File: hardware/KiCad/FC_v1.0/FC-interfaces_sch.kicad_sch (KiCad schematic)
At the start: 39 parts, among them J10 PAD_OUT, J11 PAD_OUT, J12 PAD_OUT_Mini, J13 PAD_OUT_Mini, J2 MEM2061-01-188-00-A, J3 USB4105-GF-A, J4 Conn_ARM_SWD_TagConnect_TC203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, J5 SM06B-GHS-TB, J6 SM04B-GHS-TB, J7 SM06B-GHS-TB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

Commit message: Top/Bot pours
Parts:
- removed J12, J13: PAD_OUT_Mini, FC-FootprintLib:Mini_Pad_out_1x6, symbol Connector:Conn_01x06_Socket
- added J12, J13: PAD_OUT_Mini, FC-FootprintLib:Pad_out_mini_1x4, symbol Connector:Conn_01x04_Socket
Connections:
- net ADC_IN1: now also J13.4 (Pin_4)
- net ADC_IN2: now also J13.2 (Pin_2)
- net ADC_IN3: now also J13.3 (Pin_3)
- net UART5_RX: now also J12.1 (Pin_1)
- net UART5_TX: now also J12.2 (Pin_2)
- new net GPIO_68: J12.3 (Pin_3)
- new net GPIO_69: J12.4 (Pin_4)
- new net GPIO_70: J13.1 (Pin_1)

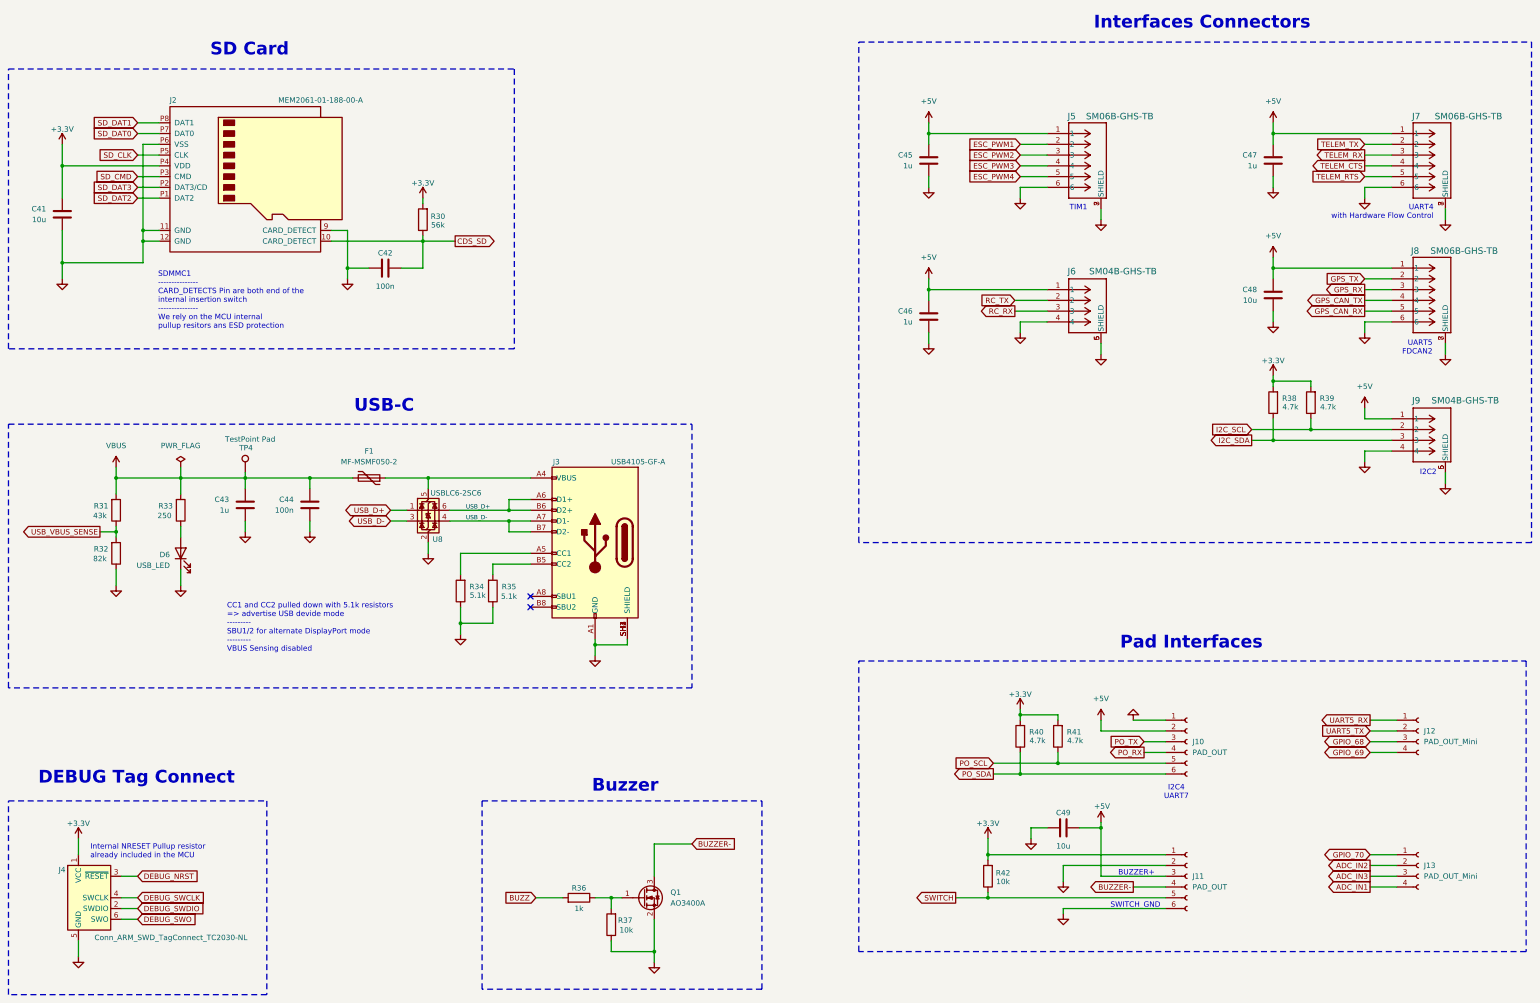
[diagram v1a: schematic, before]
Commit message: Pinout / DRC check
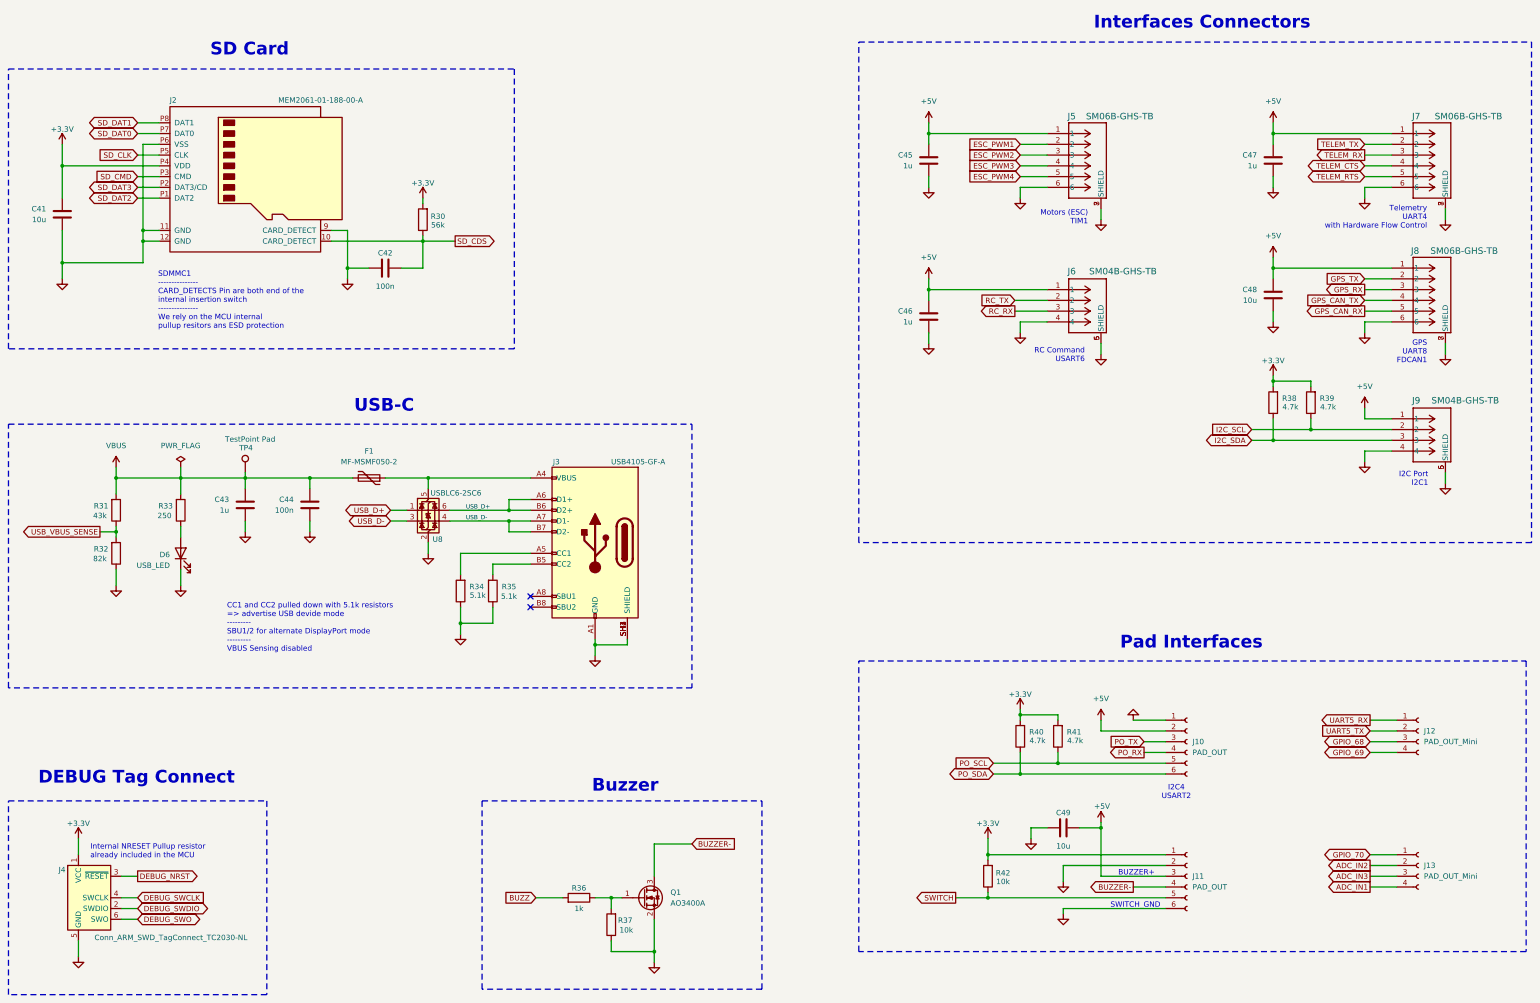
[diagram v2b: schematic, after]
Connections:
- net CDS_SD renamed SD_CDS
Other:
- note added: "GPS UART8 FDCAN1"
- note added: "I2C Port I2C1"
- note added: "I2C4 USART2"
- note added: "Motors (ESC) TIM1"
- note added: "RC Command USART6"
- note added: "Telemetry UART4 with Hardware Flow Control"
- note removed: "I2C2"
- note removed: "I2C4 UART7"
- note removed: "TIM1"
- note removed: "UART4 with Hardware Flow Control"
- note removed: "UART5 FDCAN2"
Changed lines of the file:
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@@
 	(title_block
 		(title "FC Interface Section")
-		(date "2025-12-01")
-		(rev "v0.5")
+		(date "2026-01-03")
+		(rev "v0.7")
 		(company "Guilhem Andrieu")
 	)
@@
 		)
 	)
-	(text "I2C2"
+	(text "I2C Port\nI2C1"
 		(exclude_from_sim no)
-		(at 373.126 133.35 0)
-		(effects
-			(font
-				(size 1.27 1.27)
-			)
+		(at 373.126 134.874 0)
+		(effects
+			(font
+				(size 1.27 1.27)
+			)
+			(justify right)
+		)
+	)
+	(text "RC Command\nUSART6"
+		(exclude_from_sim no)
+		(at 292.1 105.664 0)
+		(effects
+			(font
+				(size 1.27 1.27)
+			)
+			(justify right)
 		)
 	)
@@
 		)
 	)
-	(text "TIM1"
+	(text "Motors (ESC)\nTIM1"
 		(exclude_from_sim no)
-		(at 290.576 70.866 0)
-		(effects
-			(font
-				(size 1.27 1.27)
-			)
+		(at 292.862 73.152 0)
+		(effects
+			(font
+				(size 1.27 1.27)
+			)
+			(justify right)
 		)
 	)
@@
 		)
 	)
-	(text "I2C4\nUART7\n\n"
+	(text "I2C4\nUSART2\n\n"
 		(exclude_from_sim no)
 		(at 313.69 209.804 0)
@@
 		)
 	)
-	(text "UART4\nwith Hardware Flow Control"
+	(text "Telemetry\nUART4\nwith Hardware Flow Control"
 		(exclude_from_sim no)
-		(at 374.396 71.882 0)
-		(effects
-			(font
-				(size 1.27 1.27)
-			)
-			(justify right)
-		)
-	)
-	(text "UART5\nFDCAN2"
+		(at 372.872 73.152 0)
+		(effects
+			(font
+				(size 1.27 1.27)
+			)
+			(justify right)
+		)
+	)
+	(text "GPS\nUART8\nFDCAN1"
 		(exclude_from_sim no)
-		(at 374.142 103.886 0)
+		(at 372.872 104.902 0)
 		(effects
 			(font
@@
 	)
 	(global_label "SD_DAT1"
-		(shape input)
+		(shape bidirectional)
 		(at 68.58 50.8 180)
 		(fields_autoplaced yes)
@@
 		)
 		(property "Intersheetrefs" "${INTERSHEET_REFS}"
-			(at 57.612 50.8 0)
+			(at 56.5007 50.8 0)
 			(effects
 				(font
@@
 	)
 	(global_label "DEBUG_NRST"
-		(shape input)
+		(shape output)
 		(at 68.58 228.6 0)
 		(fields_autoplaced yes)
@@
 	)
 	(global_label "SD_DAT0"
-		(shape input)
+		(shape bidirectional)
 		(at 68.58 53.34 180)
 		(fields_autoplaced yes)
@@
 		)
 		(property "Intersheetrefs" "${INTERSHEET_REFS}"
-			(at 57.612 53.34 0)
+			(at 56.5007 53.34 0)
 			(effects
 				(font
@@
 	)
 	(global_label "DEBUG_SWDIO"
-		(shape input)
+		(shape bidirectional)
 		(at 68.58 236.22 0)
 		(fields_autoplaced yes)
@@
 		)
 		(property "Intersheetrefs" "${INTERSHEET_REFS}"
-			(at 84.6885 236.22 0)
+			(at 85.7998 236.22 0)
 			(effects
 				(font
@@
 		)
 	)
-	(global_label "CDS_SD"
+	(global_label "SD_CDS"
 		(shape output)
 		(at 143.51 78.74 0)
@@
 	)
 	(global_label "SD_DAT2"
-		(shape input)
+		(shape bidirectional)
 		(at 68.58 68.58 180)
 		(fields_autoplaced yes)
@@
 		)
 		(property "Intersheetrefs" "${INTERSHEET_REFS}"
-			(at 57.612 68.58 0)
+			(at 56.5007 68.58 0)
 			(effects
 				(font
@@
 	)
 	(global_label "I2C_SDA"
-		(shape output)
+		(shape bidirectional)
 		(at 331.47 125.73 180)
 		(fields_autoplaced yes)
@@
 		)
 		(property "Intersheetrefs" "${INTERSHEET_REFS}"
-			(at 320.8648 125.73 0)
+			(at 319.7535 125.73 0)
 			(effects
 				(font
@@
 	)
 	(global_label "PO_SDA"
-		(shape output)
+		(shape bidirectional)
 		(at 270.51 204.47 180)
 		(fields_autoplaced yes)
@@
 		)
 		(property "Intersheetrefs" "${INTERSHEET_REFS}"
-			(at 260.3886 204.47 0)
+			(at 259.2773 204.47 0)
 			(effects
 				(font
@@
 	)
 	(global_label "TELEM_CTS"
-		(shape output)
+		(shape bidirectional)
 		(at 358.14 60.96 180)
 		(fields_autoplaced yes)
@@
 		)
 		(property "Intersheetrefs" "${INTERSHEET_REFS}"
-			(at 344.995 60.96 0)
+			(at 343.8837 60.96 0)
 			(effects
 				(font
@@
 	)
 	(global_label "SD_DAT3"
-		(shape input)
+		(shape bidirectional)
 		(at 68.58 66.04 180)
 		(fields_autoplaced yes)
@@
 		)
 		(property "Intersheetrefs" "${INTERSHEET_REFS}"
-			(at 57.612 66.04 0)
+			(at 56.5007 66.04 0)
 			(effects
 				(font
@@
 	)
 	(global_label "TELEM_RTS"
-		(shape input)
+		(shape bidirectional)
 		(at 358.14 63.5 180)
 		(fields_autoplaced yes)
@@
 		)
 		(property "Intersheetrefs" "${INTERSHEET_REFS}"
-			(at 344.995 63.5 0)
+			(at 343.8837 63.5 0)
 			(effects
 				(font
@@
 	)
 	(global_label "GPS_CAN_TX"
-		(shape output)
+		(shape input)
 		(at 358.14 92.71 180)
 		(fields_autoplaced yes)
@@
 	)
 	(global_label "DEBUG_SWO"
-		(shape input)
+		(shape bidirectional)
 		(at 68.58 238.76 0)
 		(fields_autoplaced yes)
@@
 		)
 		(property "Intersheetrefs" "${INTERSHEET_REFS}"
-			(at 82.8137 238.76 0)
-			(effects
-				(font
+			(at 83.925 238.76 0)
+			(effects
+				(font
